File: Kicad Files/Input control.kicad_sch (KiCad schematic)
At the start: 37 parts

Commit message: started tidy up in control
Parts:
- gave numbers to parts that had none: 37

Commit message: work on cl
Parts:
- C2: renamed from C12; value 0.1µF -> C
- D10: renamed from D86; value RED -> LED_Small
- D11: renamed from D87; value BLUE -> LED_Small
- D9: renamed from D85; value GREEN -> LED_Small
- R17: renamed from R113; value 220 -> R_Small
- R18: renamed from R115; value 10k -> R_Small
- R19: renamed from R114; value 10k -> R_Small
- R20: renamed from R116; value 10k -> R_Small
- R21: renamed from R97; value 10k -> R_Small
- R22: renamed from R105; value 10k -> R_Small
- R23: renamed from R98; value 10k -> R_Small
- R24: renamed from R106; value 10k -> R_Small
- R25: renamed from R99; value 10k -> R_Small
- R26: renamed from R107; value 10k -> R_Small
- R27: renamed from R100; value 10k -> R_Small
- R28: renamed from R108; value 10k -> R_Small
- R29: renamed from R101; value 10k -> R_Small
- R30: renamed from R109; value 10k -> R_Small
- R31: renamed from R102; value 10k -> R_Small
- R32: renamed from R110; value 10k -> R_Small
- R33: renamed from R103; value 10k -> R_Small
- R34: renamed from R111; value 10k -> R_Small
- R35: renamed from R104; value 10k -> R_Small
- R36: renamed from R112; value 10k -> R_Small
- SW1: renamed from SW5; value WRITE -> SW_Push
- SW2: renamed from SW6; value RESET -> SW_Push
- SW3: renamed from SW4; value PROG/Man -> SW_DIP_x02
- renumbered SW2 to SW4, SW3 to SW5, U44 to U1, U48 to U2, U45 to U3, U49 to U4, U46 to U5, U47 to U6, U50 to U7

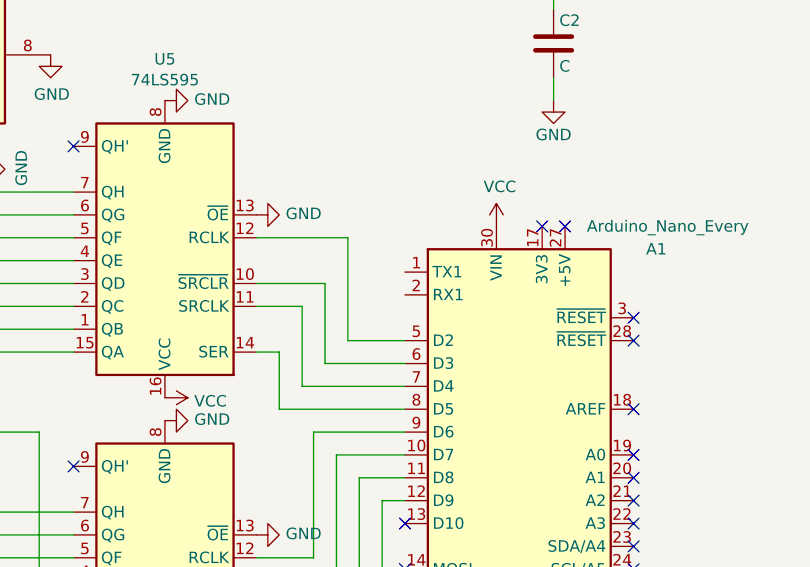
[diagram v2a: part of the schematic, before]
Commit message: fixed ecc problems
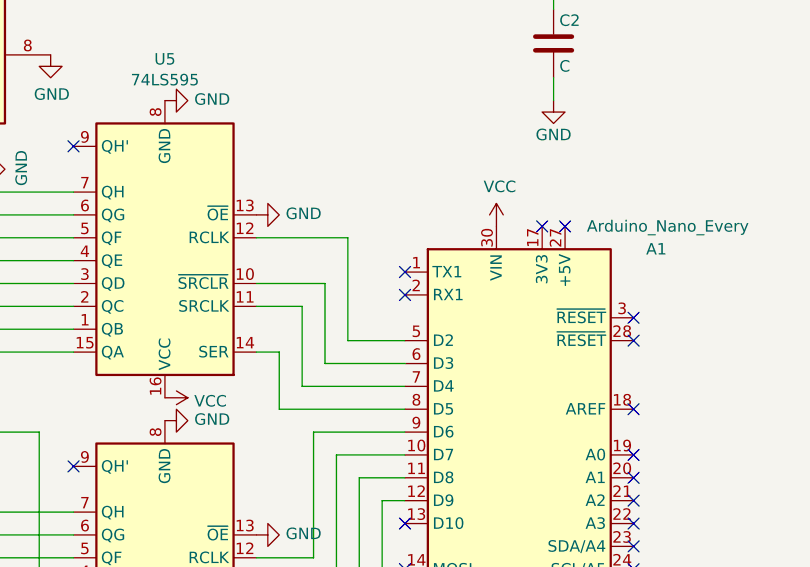
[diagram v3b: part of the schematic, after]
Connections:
- no-connect marks 19 -> 21
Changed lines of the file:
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@@
   (no_connect (at 248.92 90.17))
   (no_connect (at 186.69 53.34))
+  (no_connect (at 223.52 67.31))
+  (no_connect (at 223.52 69.85))
   (wire (pts (xy 43.18 158.75) (xy 241.3 158.75))
     (stroke (width 0) (type default) (color 0 0 0 0))

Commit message: work
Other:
- note added: "interner pullup??"
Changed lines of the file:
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@@
     (stroke (width 0) (type default) (color 0 0 0 0))
+  )
+  (text "interner pullup??" (at 54.61 52.07 0)
+    (effects (font (size 1.524 1.524)) (justify left bottom))
   )
   (text "Manual" (at 62.23 151.13 0)
@@
     (effects (font (size 1.524 1.524)) (justify left bottom))
   )
+  (text "interner pullup??" (at 54.61 119.38 0)
+    (effects (font (size 1.524 1.524)) (justify left bottom))
+  )

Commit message: w1
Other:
- moved on the sheet: A1, C2, R17, R18, R19, R20, R21, R22, R23, R24, R25, R26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
